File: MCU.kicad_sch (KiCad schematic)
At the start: 1 part, among them U1 NRF52832-QFAB-R

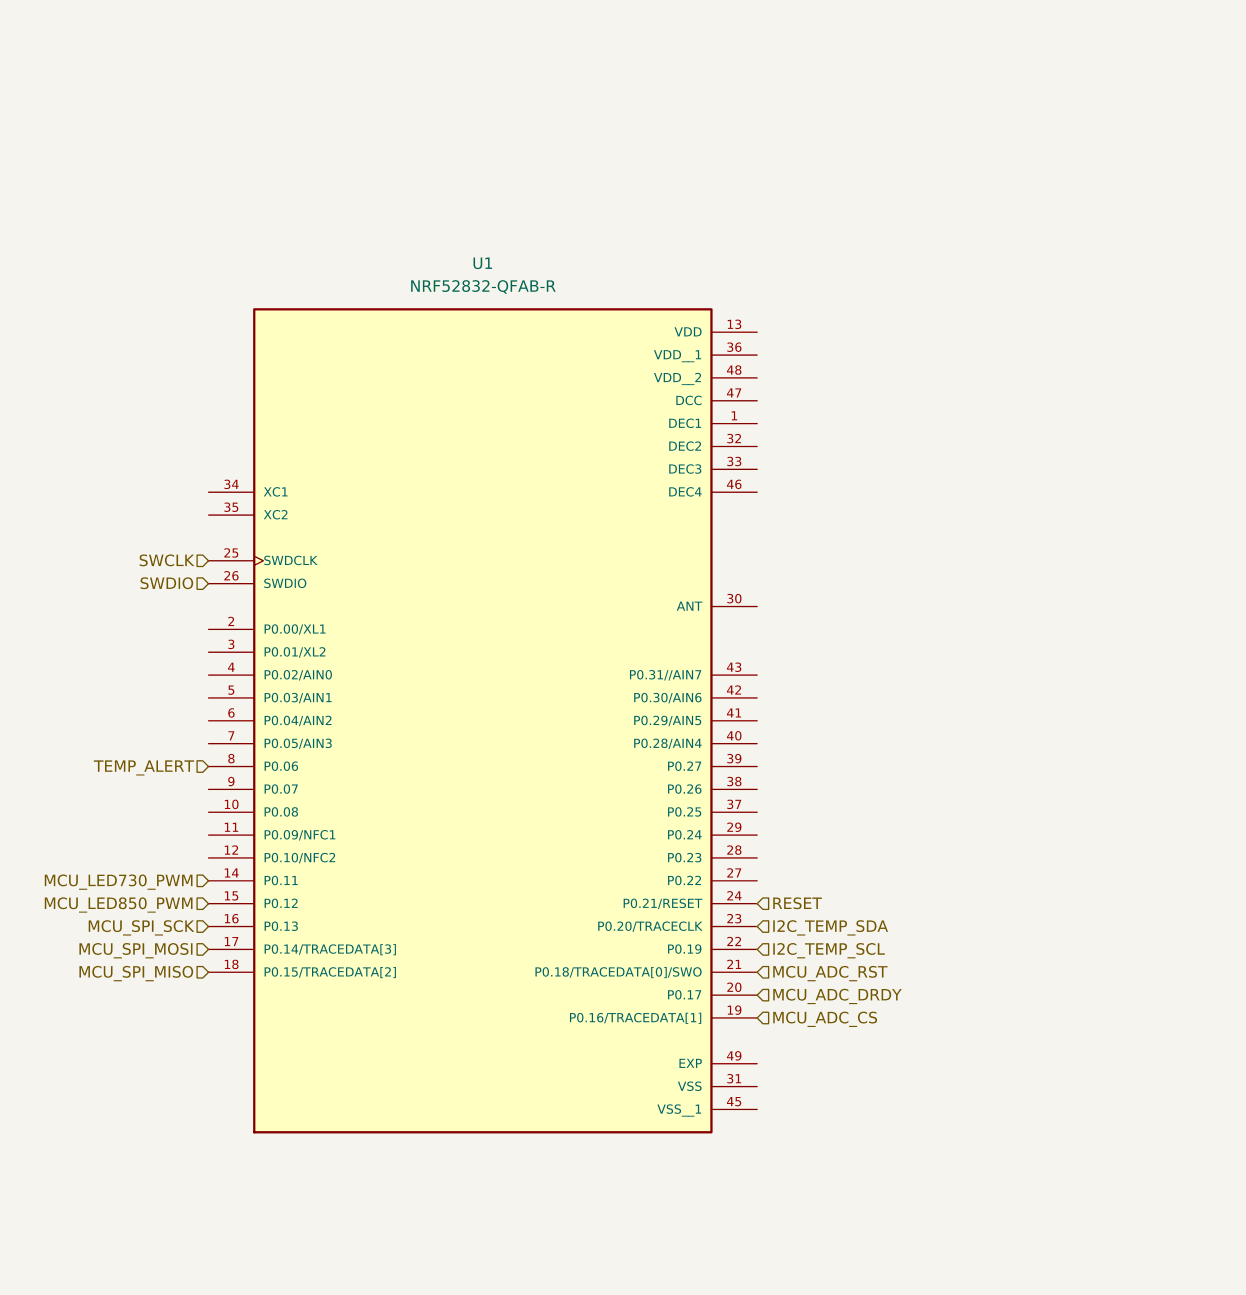
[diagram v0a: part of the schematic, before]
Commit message: change of MCU
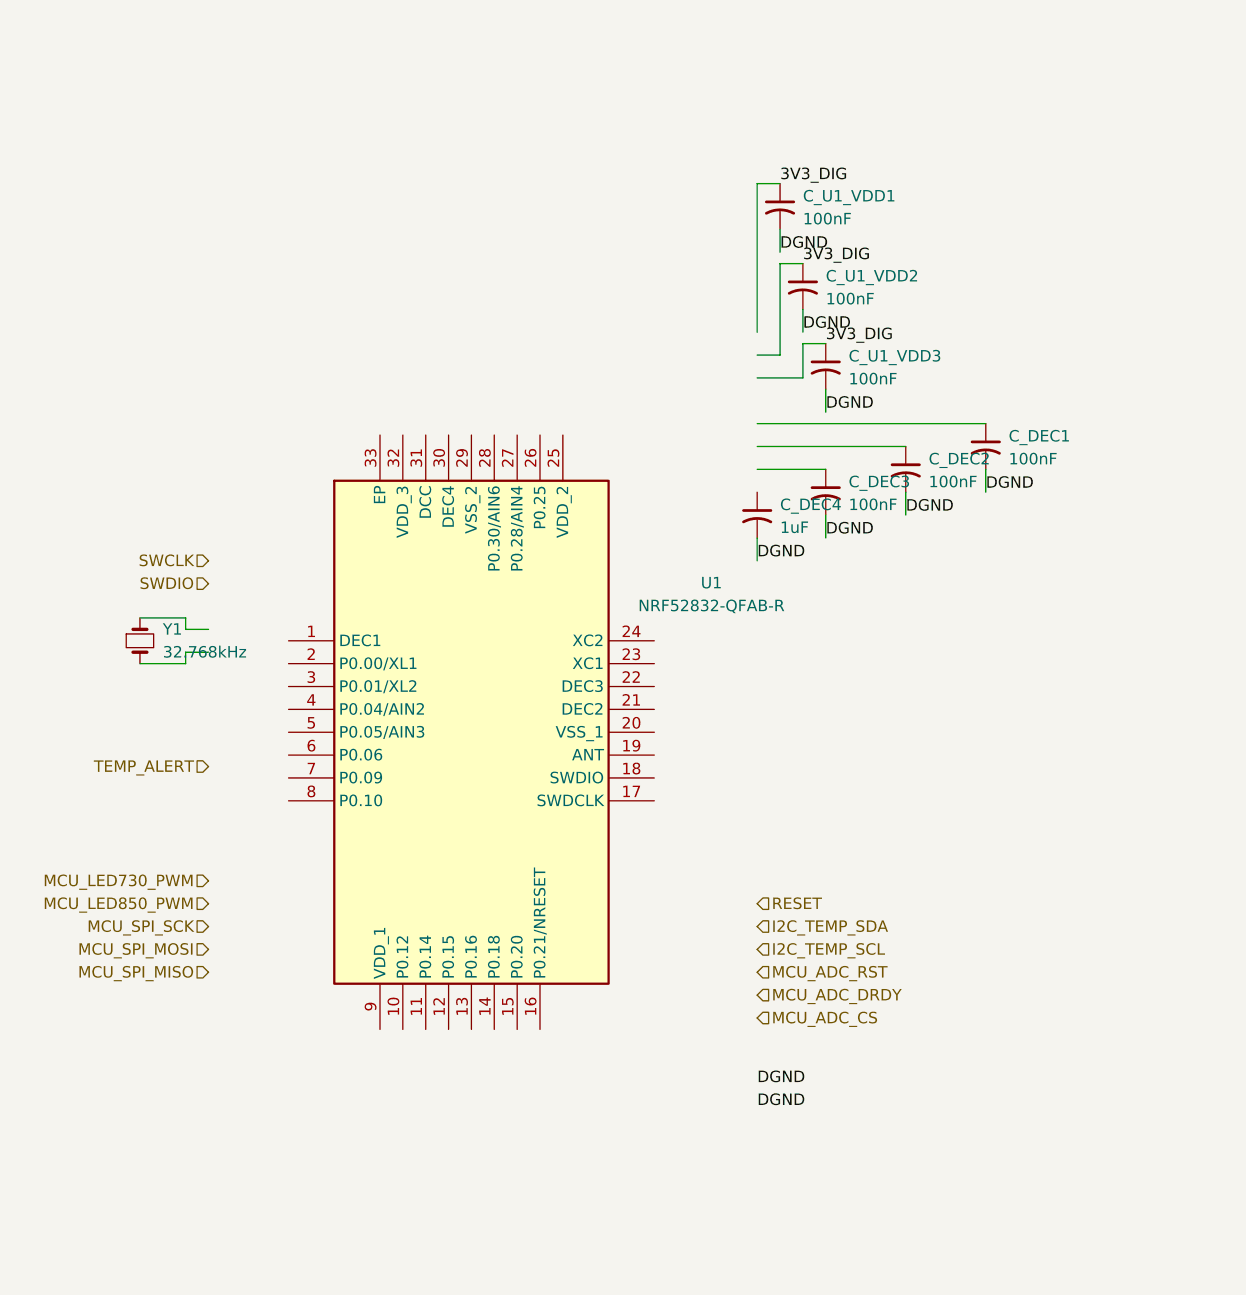
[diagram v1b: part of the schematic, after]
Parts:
- added C_DEC1, C_DEC2, C_DEC3, C_U1_VDD1, C_U1_VDD2, C_U1_VDD3: 100nF, symbol Device:C_Small_US
- added C_DEC4: 1uF, symbol Device:C_Small_US
- added Y1: 32.768kHz, symbol Device:Crystal_Small
- U1: footprint NRF52832-QFAB-R:QFN40P600X600X90-49N -> QFN50P500X500X90-33N; symbol NRF52832-QFAB-R:NRF52832-QFAB-R -> NRF52810-QCAA-E-R7:NRF52810-QCAA-E-R7; Arrow Part Number (none) -> NRF52810-QCAA-E-R7; Arrow Price/Stock (none) -> https://www.arrow.com/en/products/nrf52810-qcaa-e-r7/nordic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; Height (none) -> 0.9; Manufacturer_Name (none) -> Nordic Semiconductor; Manufacturer_Part_Number (none) -> NRF52810-QCAA-E-R7; Mouser Part Number (none) -> 949-NRF52810-QCAAER7; Mouser Price/Stock (none) -> https://www.mouser.co.uk/ProductDetail/Nordic-Semiconductor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
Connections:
- net I2C_TEMP_SCL: no longer U1.22 (P0.19)
- net I2C_TEMP_SDA: no longer U1.23 (P0.20/TRACECLK)
- net MCU_ADC_CS: no longer U1.19 (P0.16/TRACEDATA[1])
- net MCU_ADC_DRDY: no longer U1.20 (P0.17)
- net MCU_ADC_RST: no longer U1.21 (P0.18/TRACEDATA[0]/SWO)
- net MCU_LED730_PWM: no longer U1.14 (P0.11)
- net MCU_LED850_PWM: no longer U1.15 (P0.12)
- net MCU_SPI_MISO: no longer U1.18 (P0.15/TRACEDATA[2])
- net MCU_SPI_MOSI: no longer U1.17 (P0.14/TRACEDATA[3])
- net MCU_SPI_SCK: no longer U1.16 (P0.13)
- net RESET: no longer U1.24 (P0.21/RESET)
- net SWCLK: no longer U1.25 (SWDCLK)
- net SWDIO: no longer U1.26 (SWDIO)
- net TEMP_ALERT: no longer U1.8 (P0.06)
- new net 3V3_DIG: C_U1_VDD1.1, C_U1_VDD2.1, C_U1_VDD3.1
- new net DGND: C_DEC1.2, C_DEC2.2, C_DEC3.2, C_DEC4.2, C_U1_VDD1.2, C_U1_VDD2.2, C_U1_VDD3.2

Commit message: mcu ready except antenna
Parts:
- removed C_DEC3: 100nF, symbol Device:C_Small_US
- removed C_DEC4: 1uF, symbol Device:C_Small_US
- added C11, C12, C13, C14: 12pF, symbol Device:C_Small_US
- added C16: 100nF, symbol Device:C_Small_US
- added C18: 4.7uF, symbol Device:C_Small_US
- added C3: 0.8pF, symbol Device:C_Small_US
- added J_PROG1: TC2030-IDC-NL, TC2030-IDC-NL, symbol Connector_Generic:Conn_01x06
- added Y2: 32MHz, symbol Device:Crystal_Small
- C21: renamed from C_U1_VDD3; value 100nF -> 1uF
- U1: value NRF52832-QFAB-R -> NRF52810-QCAA-E-R7
- renumbered C_U1_VDD1 to C17, C_DEC1 to C19, C_U1_VDD2 to C20, C_DEC2 to C22
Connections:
- net 3V3_DIG: now also U1.25 (VDD_2), U1.32 (VDD_3), U1.9 (VDD_1), C16.1, C18.2, J_PROG1.1 (Pin_1); no longer C20.1, C21.1
- net I2C_TEMP_SCL: now also U1.4 (P0.04/AIN2)
- net I2C_TEMP_SDA: now also U1.5 (P0.05/AIN3)
- net MCU_LED730_PWM: now also U1.7 (P0.09)
- net MCU_LED850_PWM: now also U1.8 (P0.10)
- net RESET: now also U1.16 (P0.21/NRESET), J_PROG1.6 (Pin_6)
- net SWDIO: now also U1.18 (SWDIO), J_PROG1.2 (Pin_2)
- net TEMP_ALERT: now also U1.6 (P0.06)
- net at Y1.1: now also U1.2 (P0.00/XL1), C11.1
- net at Y1.2: now also U1.3 (P0.01/XL2), C12.1
- net at U1.1 (DEC1): now also C19.1
- net SWDCLK: now reaches U1.17 (SWDCLK)
- net SWDCLK: now also J_PROG1.4 (Pin_4)
- net at U1.19 (ANT): now also C3.1
- net GND: now reaches U1.20 (VSS_1)
- net GND: now also C17.2, C19.2, C20.2, C21.2, C22.1, U1.29 (VSS_2), U1.33 (EP), C11.2, C12.2, C13.2, C14.2, C16.2, C18.1, C3.2, J_PROG1.3 (Pin_3), J_PROG1.5 (Pin_5)
- net at U1.21 (DEC2): now also C20.1
- net at U1.22 (DEC3): now also C21.1
- net at U1.23 (XC1): now also C14.1, Y2.2
- net at U1.24 (XC2): now also C13.1, Y2.1
- net at U1.30 (DEC4): now also C22.2
- removed net DGND: C17.2, C19.2, C20.2, C21.2, C22.2
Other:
- moved on the sheet: C17, C19, C20, C21, C22, Y1

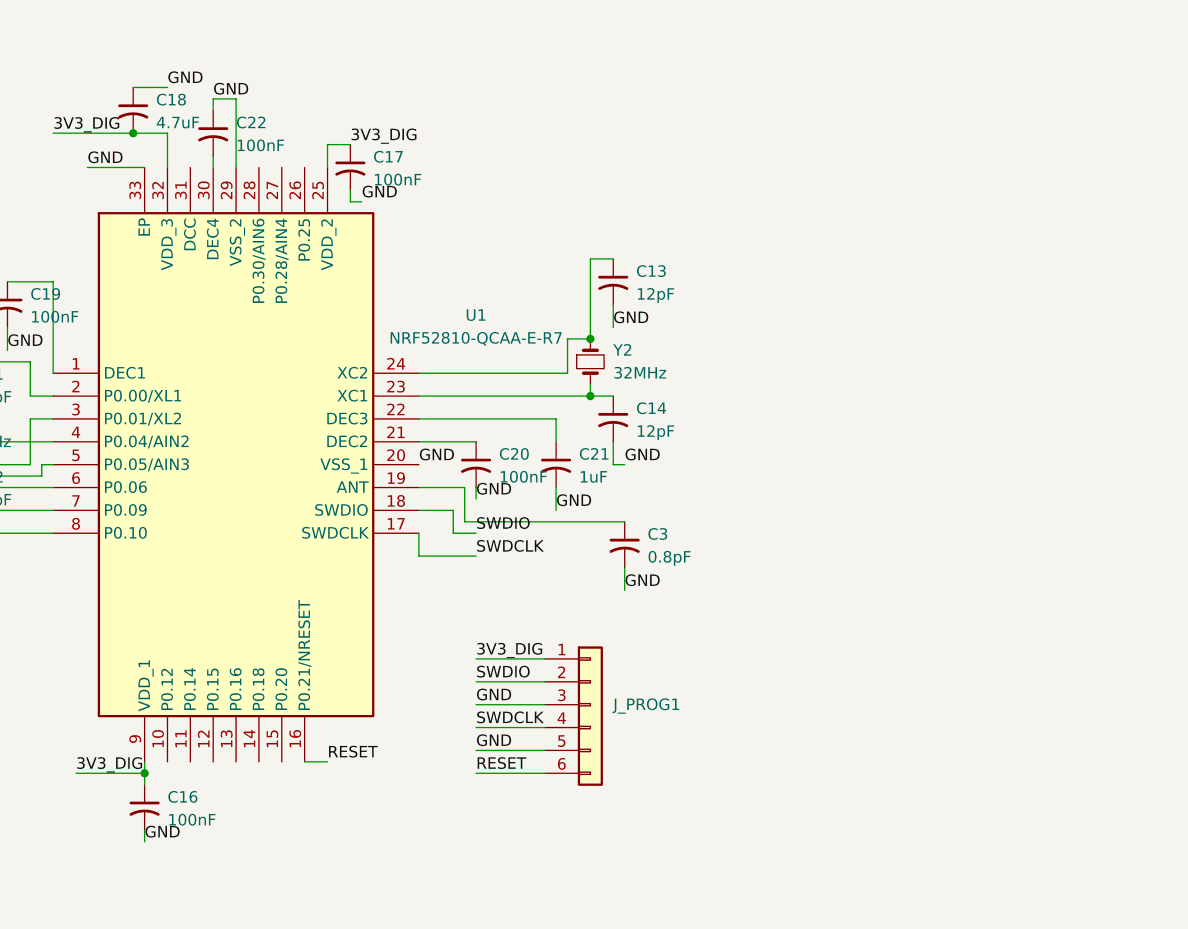
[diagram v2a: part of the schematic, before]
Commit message: mcu ready antenna
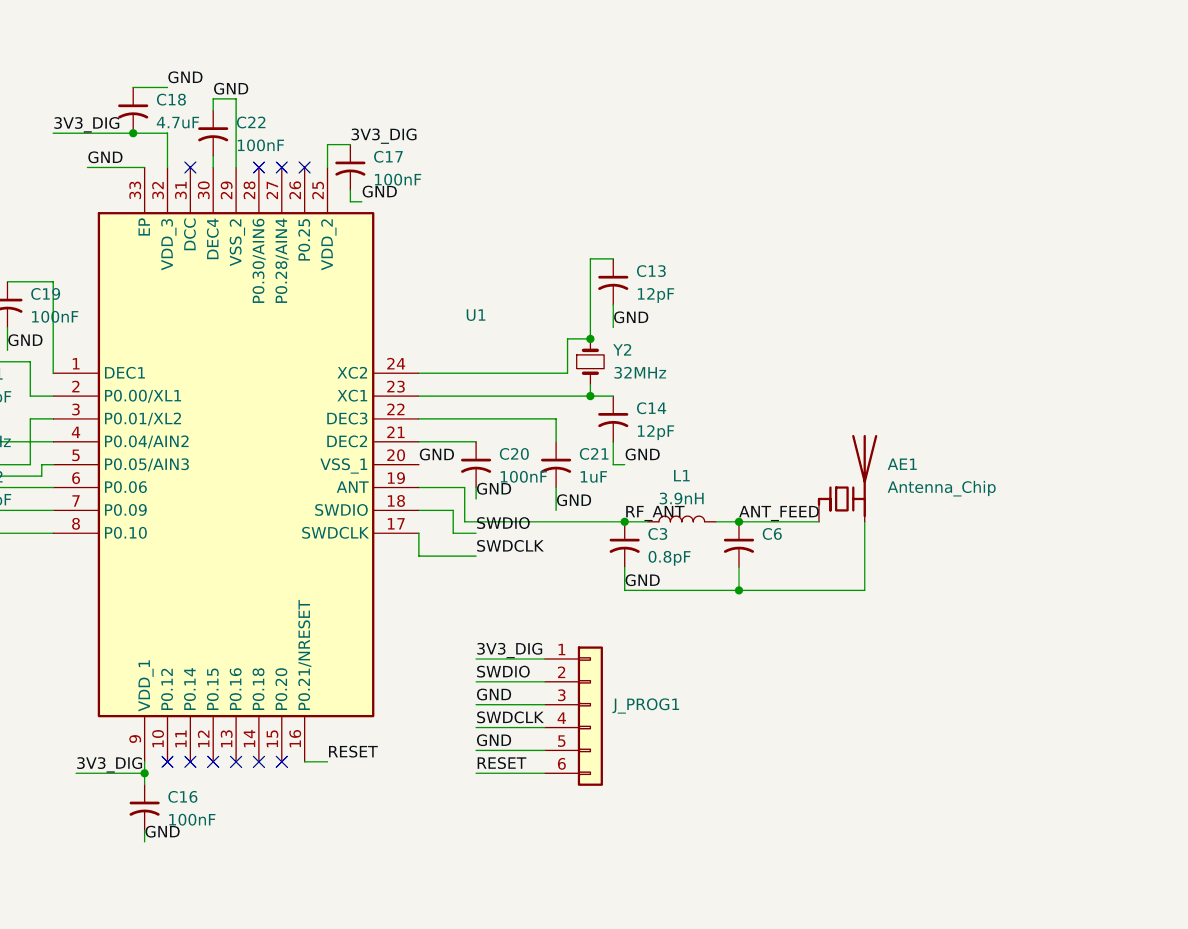
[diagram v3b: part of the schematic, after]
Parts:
- added AE1: Antenna_Chip, symbol Device:Antenna_Chip
- added C6: Not mounted, symbol Device:C_Small_US
- added L1: 3.9nH, symbol Device:L
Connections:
- net GND: now also AE1.2 (PCB_Trace), C6.2
- net RF_ANT: now reaches C3.1, U1.19 (ANT)
- net RF_ANT: now also L1.1
- new net ANT_FEED: AE1.1 (FEED), C6.1, L1.2
- no-connect marks 0 -> 10

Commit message: footprint
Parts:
- added R1, R2: 4.7k, symbol Device:R_Small_US
- U1: footprint QFN50P500X500X90-33N -> NRF52810-QCAA-E-R7:QFN50P500X500X90-33N
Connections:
- net 3V3_DIG: now also R1.1, R2.1
- net I2C_TEMP_SCL: now also R1.2
- net I2C_TEMP_SDA: now also R2.2

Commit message: program socket for MCU footprint
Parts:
- J_PROG1: footprint TC2030-IDC-NL -> Connector:Tag-Connect_TC2030-IDC-NL_2x03_P1.27mm_Vertical
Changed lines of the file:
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@@
 			)
 		)
-		(property "Footprint" "TC2030-IDC-NL"
+		(property "Footprint" "Connector:Tag-Connect_TC2030-IDC-NL_2x03_P1.27mm_Vertical"
 			(at 186.69 120.65 0)
 			(hide yes)
